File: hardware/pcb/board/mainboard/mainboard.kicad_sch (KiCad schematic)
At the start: 145 parts, among them J1 Conn_Coaxial, J10 USB_C_Receptacle, J11 2908-05WB-MG, J2 USB_C_Receptacle_USB2.0_16P, J3 Conn_02x35_Odd_Even_MountingP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, J4 Conn_02x40_Odd_Even_MountingP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, J5 Conn_02x40_Odd_Even_MountingP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, J7 Conn_01x30, J8 Conn_01x30, Q1 BSS138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

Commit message: I2C cam0 cam1
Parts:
- added R37: 0, Resistor_SMD:R_0603_1608Metric, symbol Device:R_Small
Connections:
- net B+: no longer C12.1, TP7.1, U4.13 (BAT), U4.14 (BAT)
- net CAM0_RESET: now also R37.1; no longer J8.24 (Pin_24)
- net B+ after curr_sense: now reaches C9.1, R4.2, U5.6 (BAT), U5.8 (SRP)
- net B+ after curr_sense: now also C12.1, TP7.1, U4.13 (BAT), U4.14 (BAT)
- new net: J8.24 (Pin_24), R37.2
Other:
- moved on the sheet: TP7
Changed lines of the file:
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@@
 	)
 	(junction
+		(at 99.06 78.74)
+		(diameter 0)
+		(color 0 0 0 0)
+	)
+	(junction
 		(at 196.85 55.88)
 		(diameter 0)
@@
 	)
 	(junction
-		(at 99.06 80.01)
-		(diameter 0)
-		(color 0 0 0 0)
-	)
-	(junction
 		(at 68.58 38.1)
 		(diameter 0)
@@
 	(wire
 		(pts
-			(xy 99.06 80.01) (xy 99.06 82.55)
+			(xy 99.06 78.74) (xy 99.06 82.55)
 		)
 		(stroke
@@
 	(wire
 		(pts
+			(xy 483.87 354.33) (xy 485.14 354.33)
+		)
+		(stroke
+			(width 0)
+			(type default)
+		)
+	)
+	(wire
+		(pts
 			(xy 90.17 69.85) (xy 99.06 69.85)
 		)
@@
 	(wire
 		(pts
-			(xy 99.06 80.01) (xy 99.06 69.85)
+			(xy 490.22 354.33) (xy 500.38 354.33)
 		)
 		(stroke
@@
 	(wire
 		(pts
+			(xy 99.06 78.74) (xy 99.06 69.85)
+		)
+		(stroke
+			(width 0)
+			(type default)
+		)
+	)
+	(wire
+		(pts
 			(xy 88.9 44.45) (xy 100.33 44.45)
 		)
@@
 		)
 	)
+	(global_label "B+ after curr_sense"
+		(shape input)
+		(at 144.78 57.15 90)
+		(fields_autoplaced yes)
+		(effects
+			(font
+				(size 1.27 1.27)
+			)
+			(justify left)
+		)
+		(property "Intersheetrefs" "${INTERSHEET_REFS}"
+			(at 144.78 34.752 90)
+			(hide yes)
+			(show_name no)
+			(do_not_autoplace no)
+			(effects
+				(font
+					(size 1.27 1.27)
+				)
+				(justify left)
+			)
+		)
+	)
 	(global_label "CSI_1_CKN"
 		(shape input)
@@
 	(global_label "CAM1_RESET"
 		(shape input)
-		(at 500.38 354.33 180)
+		(at 483.87 354.33 180)
 		(fields_autoplaced yes)
 		(effects
@@
 		)
 		(property "Intersheetrefs" "${INTERSHEET_REFS}"
-			(at 485.6626 354.33 0)
+			(at 469.1526 354.33 0)
 			(hide yes)
 			(show_name no)
@@
 		)
 	)
-	(global_label "B+"
+	(global_label "B+ after curr_sense"
 		(shape input)
-		(at 99.06 82.55 180)
+		(at 99.06 82.55 0)
 		(fields_autoplaced yes)
 		(effects
@@
 				(size 1.27 1.27)
 			)
-			(justify right)
+			(justify left)
 		)
 		(property "Intersheetrefs" "${INTERSHEET_REFS}"
-			(at 93.2324 82.55 0)
+			(at 121.458 82.55 0)
 			(hide yes)
 			(show_name no)
@@
 					(size 1.27 1.27)
 				)
-				(justify right)
+				(justify left)
 			)
 		)
@@
 	(symbol
 		(lib_id "Connector:TestPoint")
-		(at 99.06 80.01 270)
+		(at 99.06 78.74 270)
 		(unit 1)
 		(body_style 1)
@@
 		(fields_autoplaced yes)
 		(property "Reference" "TP7"
-			(at 103.759 78.7978 90)
+			(at 103.759 77.5278 90)
 			(show_name no)
 			(do_not_autoplace no)
@@
 		)
 		(property "Value" "TestPoint"
-			(at 103.759 81.2221 90)
+			(at 103.759 79.9521 90)
 			(show_name no)
 			(do_not_autoplace no)
@@
 		)
 		(property "Footprint" "TestPoint:TestPoint_Pad_D1.5mm"
-			(at 99.06 85.09 0)
+			(at 99.06 83.82 0)
 			(hide yes)
 			(show_name no)
@@
 		)
 		(property "Datasheet" ""
-			(at 99.06 85.09 0)
+			(at 99.06 83.82 0)
 			(hide yes)
 			(show_name no)
@@
 		)
 		(property "Description" "test point"
-			(at 99.06 80.01 0)
+			(at 99.06 78.74 0)
 			(hide yes)
 			(show_name no)
@@
 		)
 		(property "Value" "10 mΩ, 1%"
-			(at 140.462 54.864 90)
+			(at 132.334 54.102 90)
 			(show_name no)
 			(do_not_autoplace no)
@@
 					(unit 1)
 				)
+			)
+		)
+	)
+	(symbol
+		(lib_id "Device:R_Small")
+		(at 487.68 354.33 90)
+		(unit 1)
+		(body_style 1)
+		(exclude_from_sim no)
+		(in_bom yes)
+		(on_board yes)
+		(in_pos_files yes)
+		(dnp no)
+		(property "Reference" "R37"
+			(at 487.68 356.362 90)
+			(show_name no)
+			(do_not_autoplace no)
+			(effects
+				(font
+					(size 1.27 1.27)
+				)
+			)
+		)
+		(property "Value" "0"
+			(at 487.68 358.7863 90)
+			(show_name no)
+			(do_not_autoplace no)
+			(effects
+				(font
+					(size 1.27 1.27)
+				)
+			)
+		)
+		(property "Footprint" "Resistor_SMD:R_0603_1608Metric"
+			(at 487.68 354.33 0)
+			(hide yes)
+			(show_name no)
+			(do_not_autoplace no)
+			(effects
+				(font
+					(size 1.27 1.27)
+				)
+			)
+		)
+		(property "Datasheet" ""
+			(at 487.68 354.33 0)
+			(hide yes)
+			(show_name no)
+			(do_not_autoplace no)
+			(effects
+				(font
+					(size 1.27 1.27)
+				)
+			)
+		)
+		(property "Description" "Resistor, small symbol"
+			(at 487.68 354.33 0)
+			(hide yes)
+			(show_name no)
+			(do_not_autoplace no)
+			(effects
+				(font
+					(size 1.27 1.27)
+				)
+			)
+		)
+		(pin "2"
+		)
+		(pin "1"
+		)
+		(instances
+			(project "mainboard"
+				(path "/0d10df44-32de-4e15-8354-02c97578c850"
+					(reference "R37")
+					(unit 1)
+				)

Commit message: route TPs
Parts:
- removed TP6: TestPoint, TestPoint:TestPoint_Pad_D1.5mm, symbol Connector:TestPoint
- added TP25, TP26: TestPoint, TestPoint:TestPoint_Pad_D1.5mm, symbol Connector:TestPoint
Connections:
- net SCL is gone; now on net H_I2C2_SCL: TP18.1
- net SDA is gone; now on net H_I2C2_SDA: TP16.1
- net H_I2C3_SCL: now also TP26.1
- net H_I2C3_SDA: now also TP25.1
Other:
- moved on the sheet: TP16, TP17, TP18

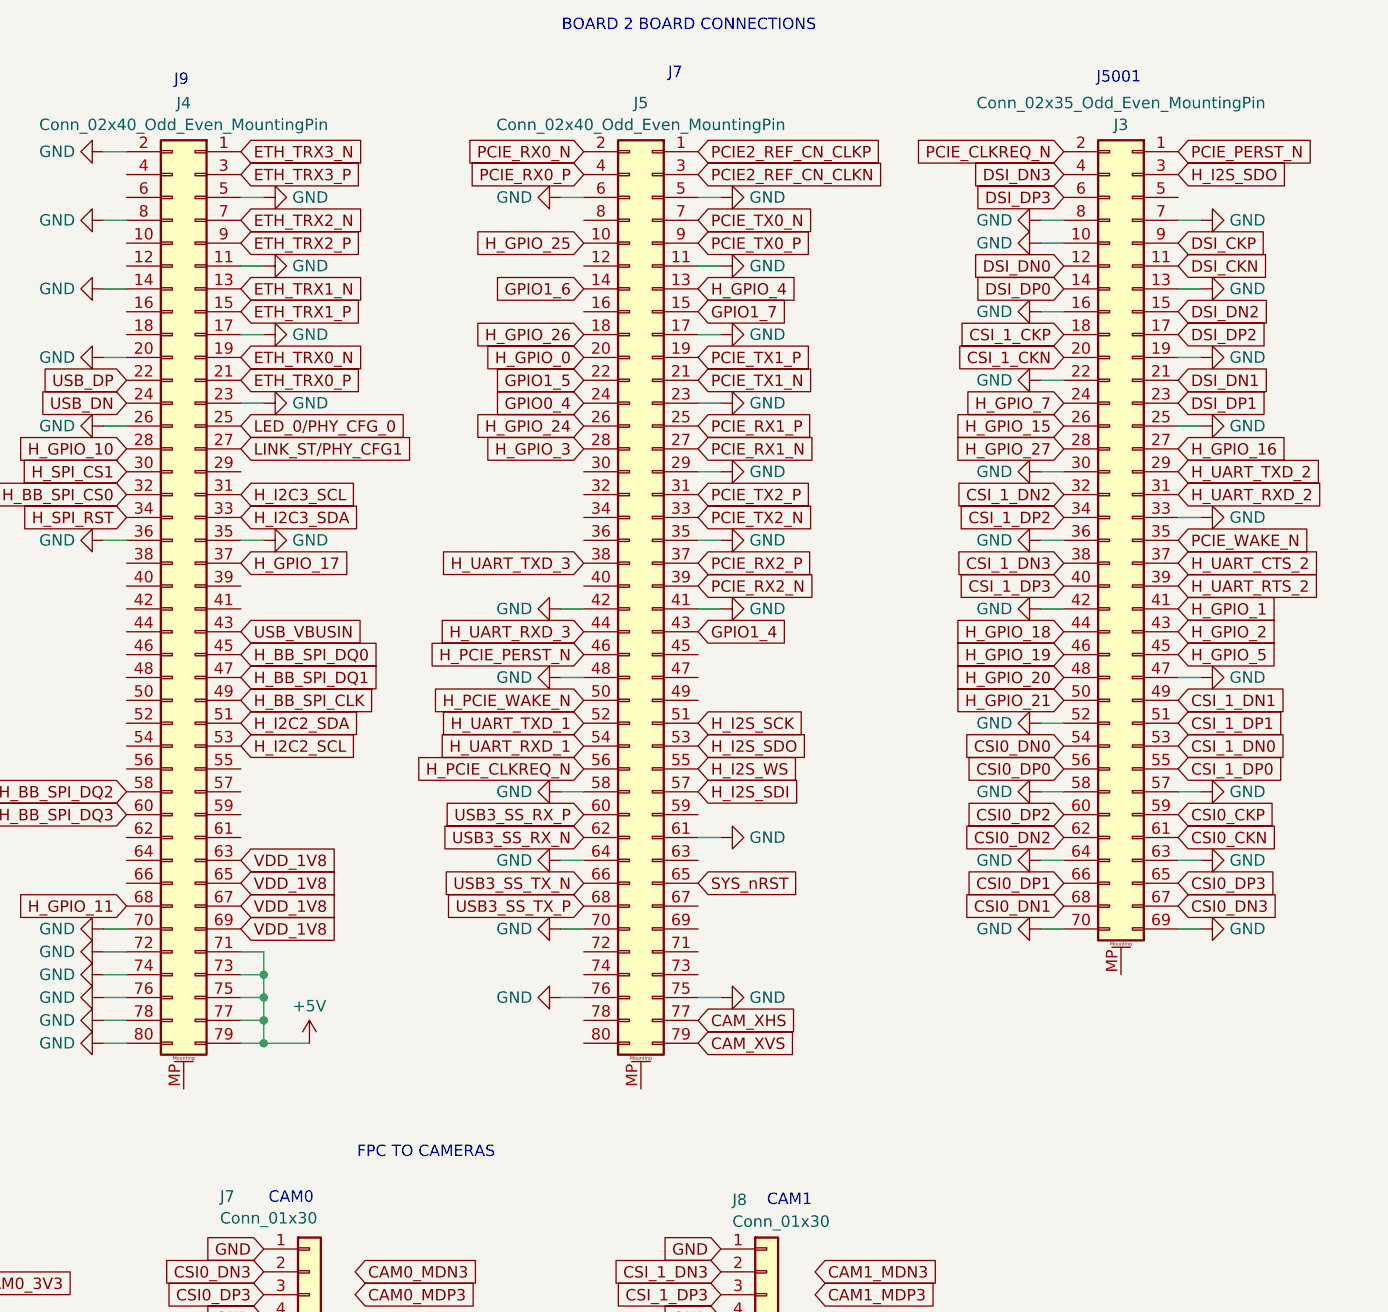
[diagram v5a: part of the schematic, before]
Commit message: 5V connection to DF40
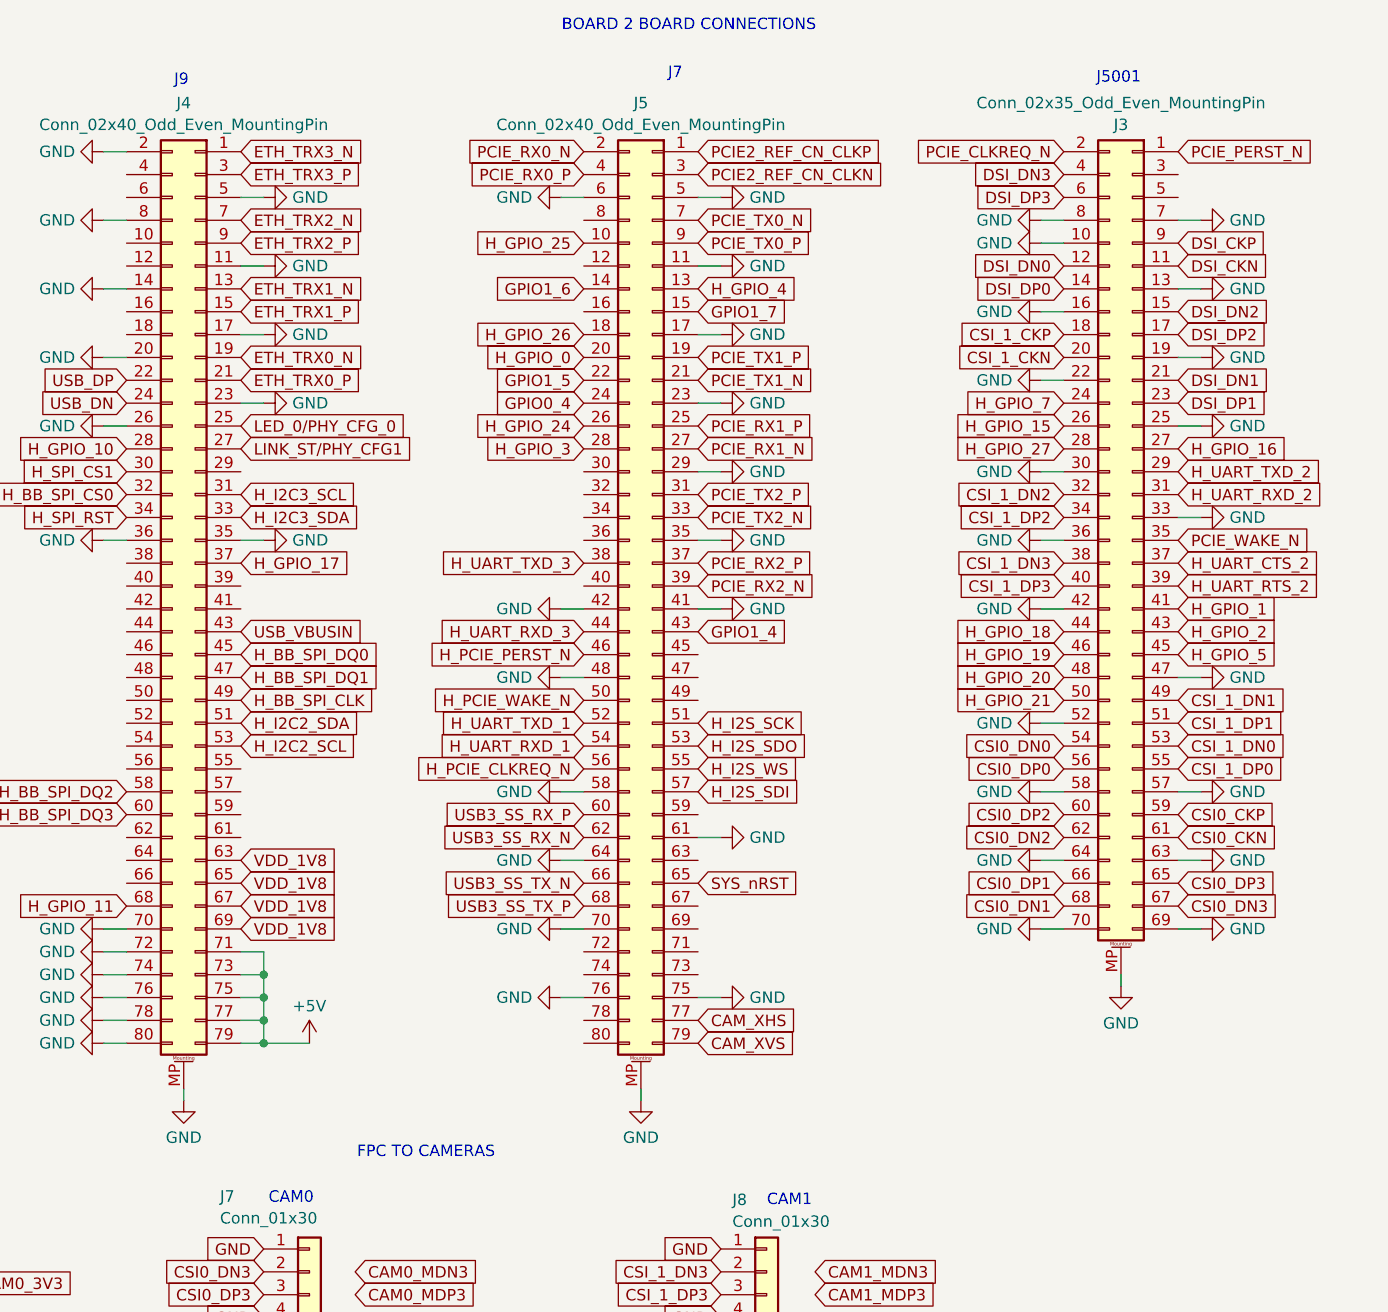
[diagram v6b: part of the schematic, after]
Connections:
- net GND: now also J3.MP (MountPin), J4.MP (MountPin), J5.MP (MountPin)
- net H_I2S_SDO: no longer J3.3 (Pin_3)

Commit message: fix drill sizes + add GND vias
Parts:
- U4: footprint Package_DFN_QFN:HVQFN-24-1EP_4x4mm_P0.5mm_EP2.6x2.6mm_ThermalVias -> unsurv_offline_pcb_footprints:HVQFN-24-1EP_4x4mm_P0.5mm_EP2.6x2.6mm_0.25drill_ThermalVias
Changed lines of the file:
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@@
 			)
 		)
-		(property "Footprint" "Package_DFN_QFN:HVQFN-24-1EP_4x4mm_P0.5mm_EP2.6x2.6mm_ThermalVias"
+		(property "Footprint" "unsurv_offline_pcb_footprints:HVQFN-24-1EP_4x4mm_P0.5mm_EP2.6x2.6mm_0.25drill_ThermalVias"
 			(at 68.58 64.77 0)
 			(hide yes)

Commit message: add on-off slider switch
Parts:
- added S1: EG1270, unsurv_offline_pcb_footprints:EG1270 switch, symbol dk_Slide-Switches:EG1218
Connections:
- net GND: now also S1.1
- net SYS: now also S1.3; no longer U9.7 (EN)
- new net: S1.2, U9.7 (EN)
